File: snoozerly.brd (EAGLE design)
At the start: 70.9 x 44 mm, 51 parts, among them Q2 MOSFET-NCHANNELFDD8780, Q3 MOSFET-NCHANNELBSS123LT1G, Q4 MOSFET-NCHANNELBSS123LT1G, U1 ATMEGA328P, Y1 32KHz, Y2 8MHz

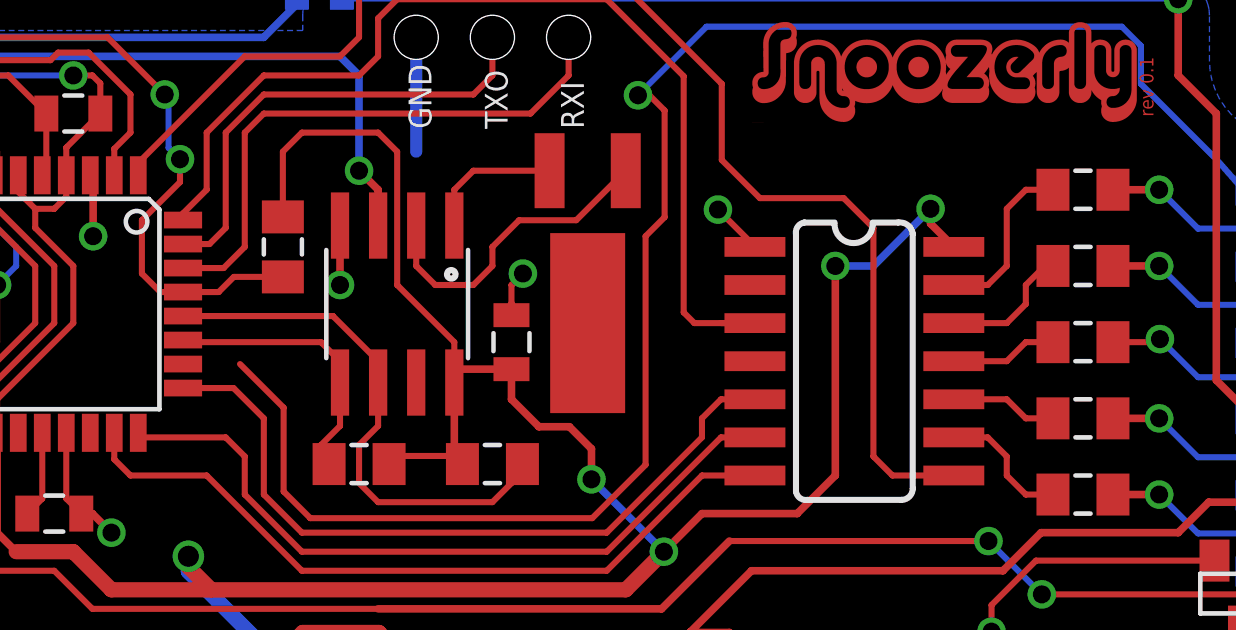
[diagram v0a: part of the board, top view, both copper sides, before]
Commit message: renamed board and schematic files
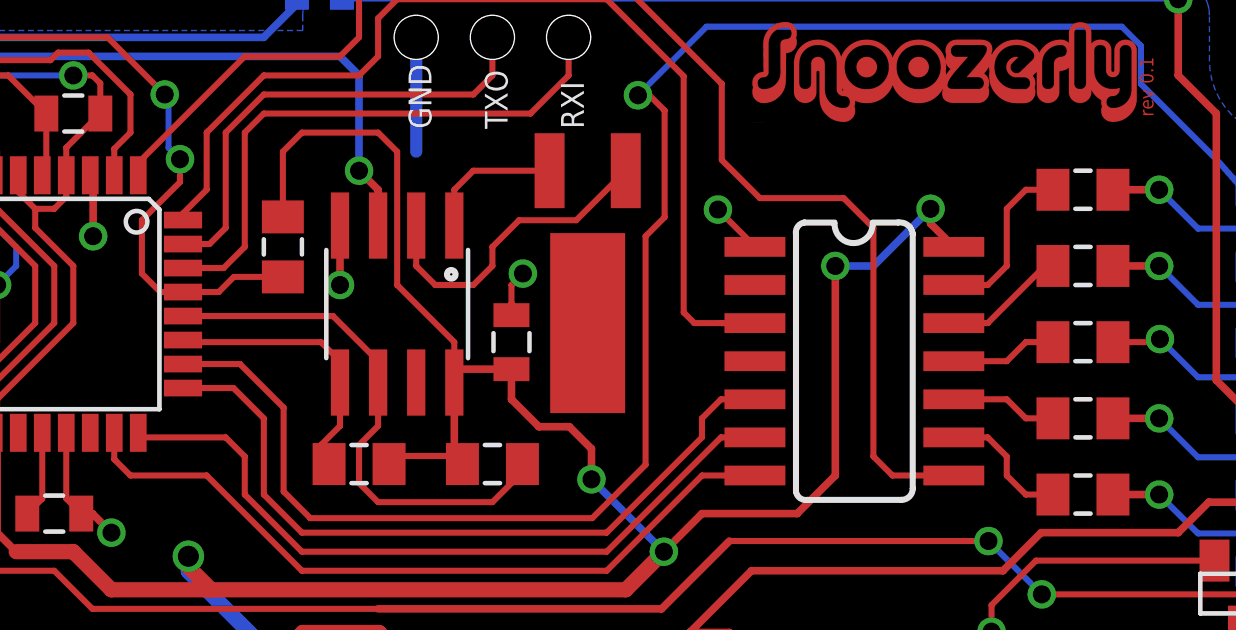
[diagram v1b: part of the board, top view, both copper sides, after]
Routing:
- net STATUS: track 56.9 -> 58.8 mm
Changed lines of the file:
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@@
 <contactref element="AT42QT1070" pad="12"/>
 <contactref element="U$8" pad="1"/>
-<wire x1="54.7243" y1="30.1244" x2="56.4896" y2="30.1244" width="0.2032" layer="1"/>
-<wire x1="56.4896" y1="30.1244" x2="57.1246" y2="30.7594" width="0.2032" layer="1"/>
-<wire x1="57.1246" y1="30.7594" x2="57.1246" y2="31.3944" width="0.2032" layer="1"/>
-<wire x1="57.1246" y1="31.3944" x2="57.7596" y2="32.0294" width="0.2032" layer="1"/>
-<wire x1="57.7596" y1="32.0294" x2="58.0296" y2="32.0294" width="0.2032" layer="1"/>
+<wire x1="58.0296" y1="32.0294" x2="57.7596" y2="32.0294" width="0.2032" layer="1"/>
+<wire x1="57.7596" y1="32.0294" x2="55.8546" y2="30.1244" width="0.2032" layer="1"/>
+<wire x1="55.8546" y1="30.1244" x2="54.7243" y2="30.1244" width="0.2032" layer="1"/>
 </signal>
 <signal name="KEY0">
@@
 <wire x1="63.5" y1="35.56" x2="64.77" y2="34.116" width="0.2032" layer="16"/>
 <wire x1="64.77" y1="34.116" x2="65.612" y2="34.544" width="0.2032" layer="16"/>
-<wire x1="30.9306" y1="28.7594" x2="29.0322" y2="28.7594" width="0" layer="19" extent="1-1"/>
+<wire x1="30.9306" y1="28.7594" x2="29.0322" y2="28.7594" width="0.2032" layer="1"/>
 </signal>
 </signals>

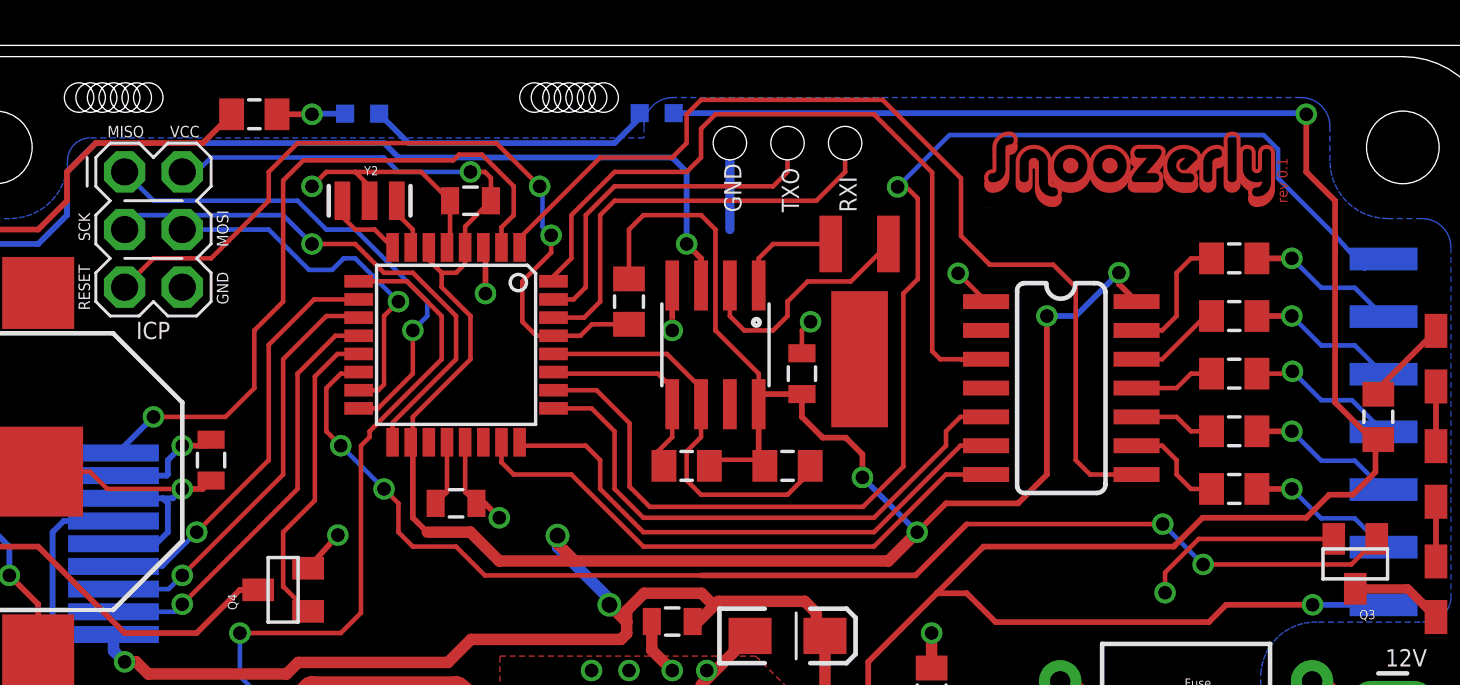
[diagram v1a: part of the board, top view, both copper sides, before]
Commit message: added output 0603 pullup resistors to touch sensor.
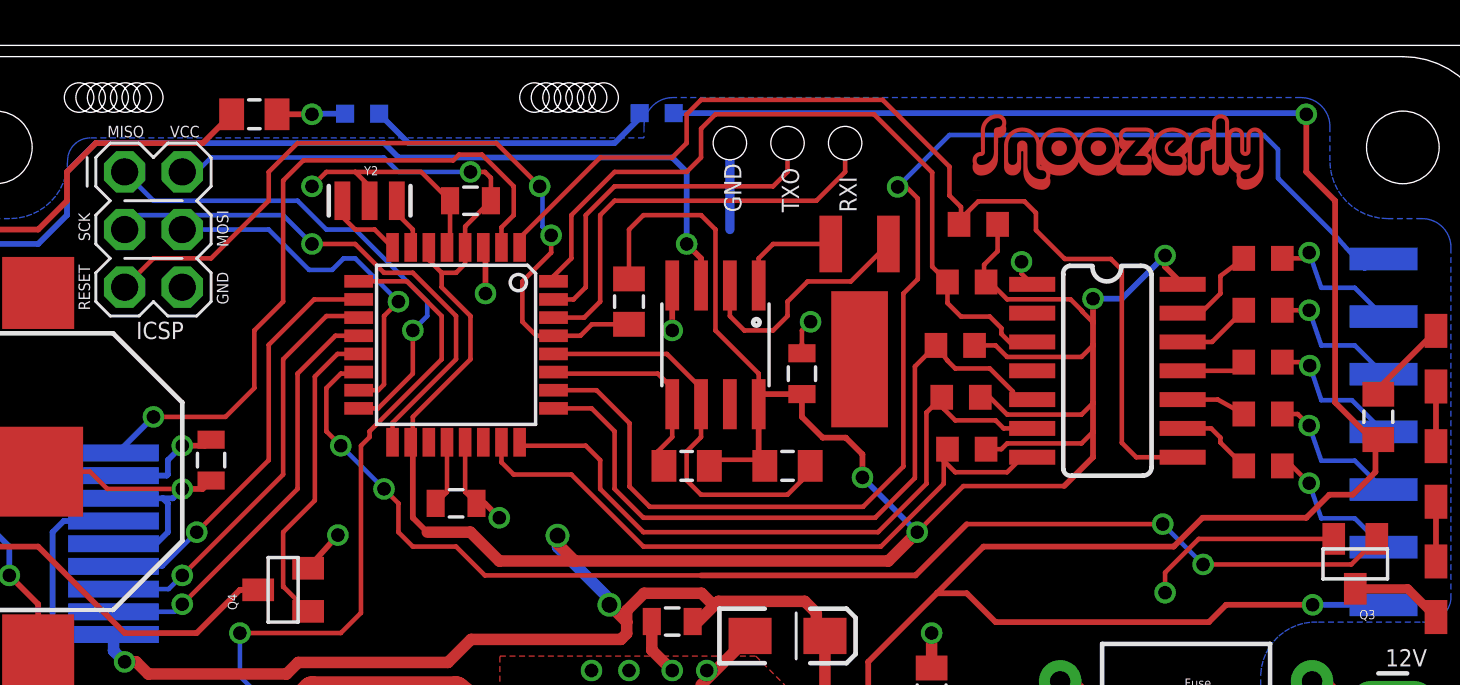
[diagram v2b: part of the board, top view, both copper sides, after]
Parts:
- added U$19: (no value), jt_parts:SNOOZERLY_TOP
- added U$21, U$22, U$23, U$24: 10k, adafruit:R0603
- U$10, U$11, U$7, U$8, U$9: device jt_parts:RESISTOR-0805 -> adafruit:R0603
- U$16: value 103 -> 100
- U$17, U$18: value 330 -> 1.3k
- U$6: value (none) -> 10k; device jt_parts:SNOOZERLY_TOP -> adafruit:R0603
- moved U$6 3.39 mm to (47.2, 33.5), turned to 180 degrees
- moved AT42QT1070 2.17 mm to (53.4, 30.3)
- moved U$11 1.63 mm to (60.3, 25.4)
- moved U$10 1.48 mm to (60.3, 27.7)
- moved U$9 1.37 mm to (60.3, 30.0)
- moved U$8 1.30 mm to (60.3, 32.3)
- moved U$7 1.27 mm to (60.3, 34.6)
- renumbered ICP to ICSP
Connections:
- net 5V: now also U$21.1, U$22.1, U$23.2, U$24.1, U$6.1
- net OUT0: now also U$6.2
- net OUT1: now also U$23.1
- net OUT2: now also U$22.2
- net OUT3: now also U$21.2
- net OUT4: now also U$24.2
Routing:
- net 5V: track 164.4 -> 191.3 mm
- net OUT4: track 24.8 -> 31.9 mm
- net OUT3: track 24.5 -> 30.1 mm
- net OUT2: track 25.1 -> 29.0 mm
- net OUT1: track 43.7 -> 46.6 mm
- net KEY0: track 6.01 -> 4.08 mm
- net KEY4: track 4.74 -> 3.50 mm
- net KEY1: track 4.09 -> 3.27 mm
- net KEY3: track 3.57 -> 2.86 mm
- net OUT0: track 34.3 -> 35.0 mm
- net KEY2: track 3.93 -> 3.36 mm
- net GND: track 115.6 -> 115.1 mm
- net N$30: track 6.65 -> 6.09 mm
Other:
- board text removed: "rev 0.1"

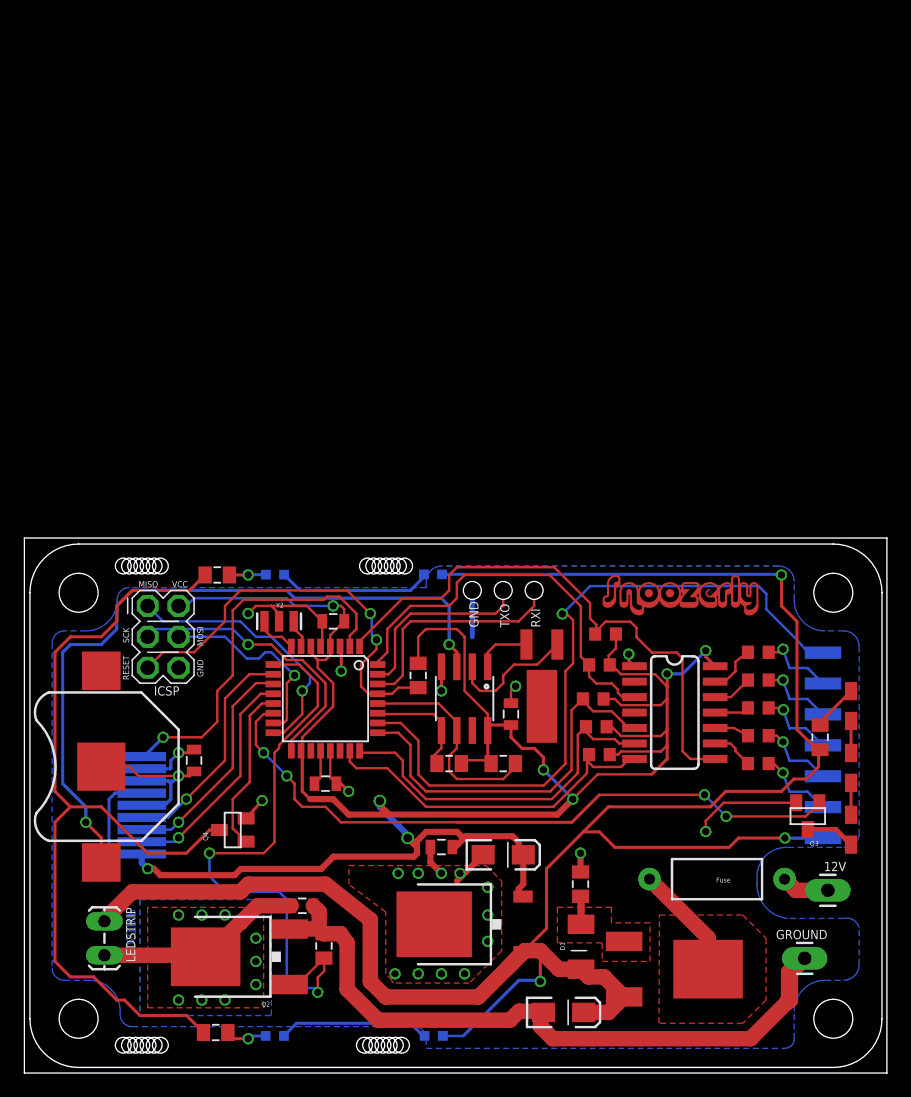
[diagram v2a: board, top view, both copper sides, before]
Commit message: Added electrolytics and snubber jumper.
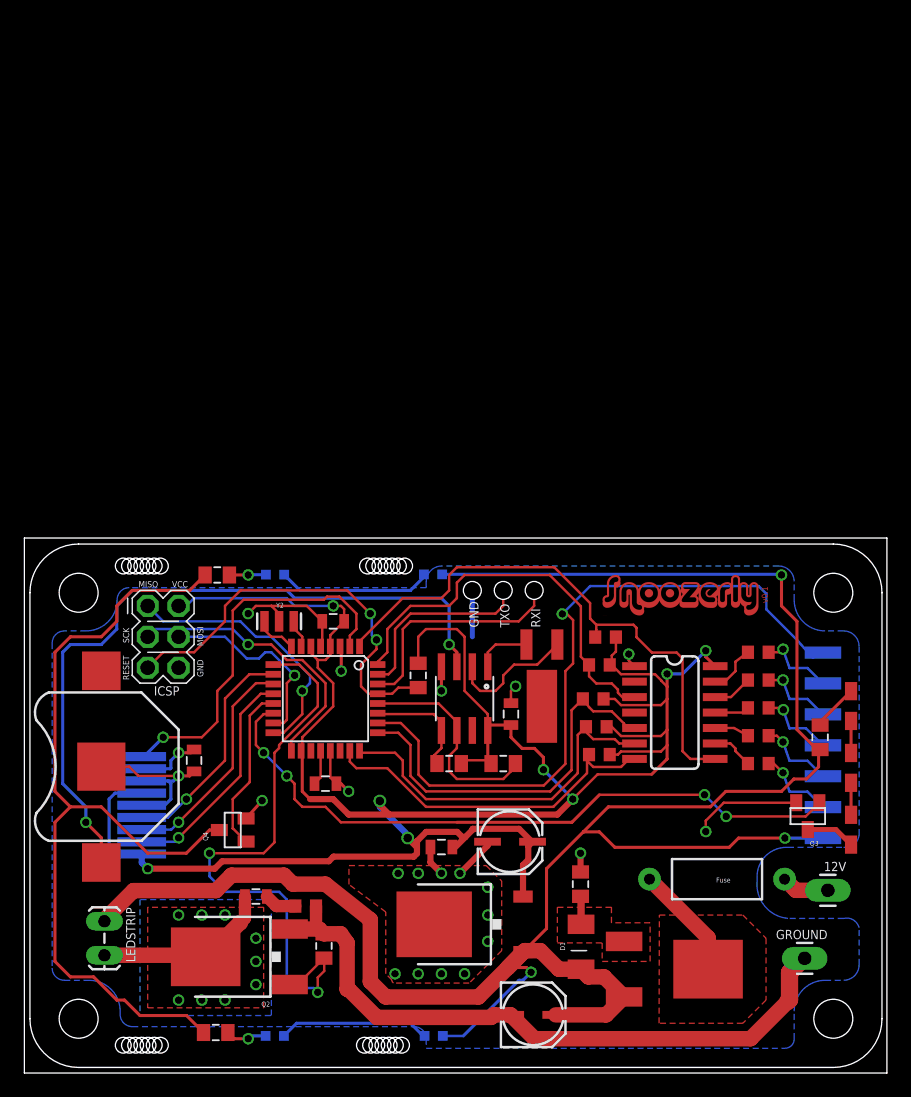
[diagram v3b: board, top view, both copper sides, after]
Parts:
- added U$25: zero, adafruit:R0603
- C5, C7: device SparkFun-Capacitors:EIA3216-KIT -> SparkFun-Capacitors:PANASONIC_C
- moved C4 3.89 mm to (19.0, 14.5)
- moved C5 2.54 mm to (41.8, 4.98)
- moved C7 1.37 mm to (39.9, 19.2)
- moved U$23 0.25 mm to (47.8, 35.8), turned to 180 degrees
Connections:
- new net N$18: C4.1, U$25.2
- net 12V: now also C5.+; no longer C5.A
- net 5V: now also C7.+, U$23.1; no longer C7.A, U$23.2
- net GND: now also C5.-, C7.-, U$25.1; no longer C4.1, C5.C, C7.C
- net OUT1: now also U$23.2; no longer U$23.1
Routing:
- net N$18: track 0.00 -> 2.67 mm
- net N$14: track 19.1 -> 16.6 mm
- net 12V: track 173.1 -> 175.0 mm
- net GND: track 115.1 -> 113.9 mm
- net 5V: track 191.3 -> 192.1 mm
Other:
- board text added: "v0.1"

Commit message: added top control board.
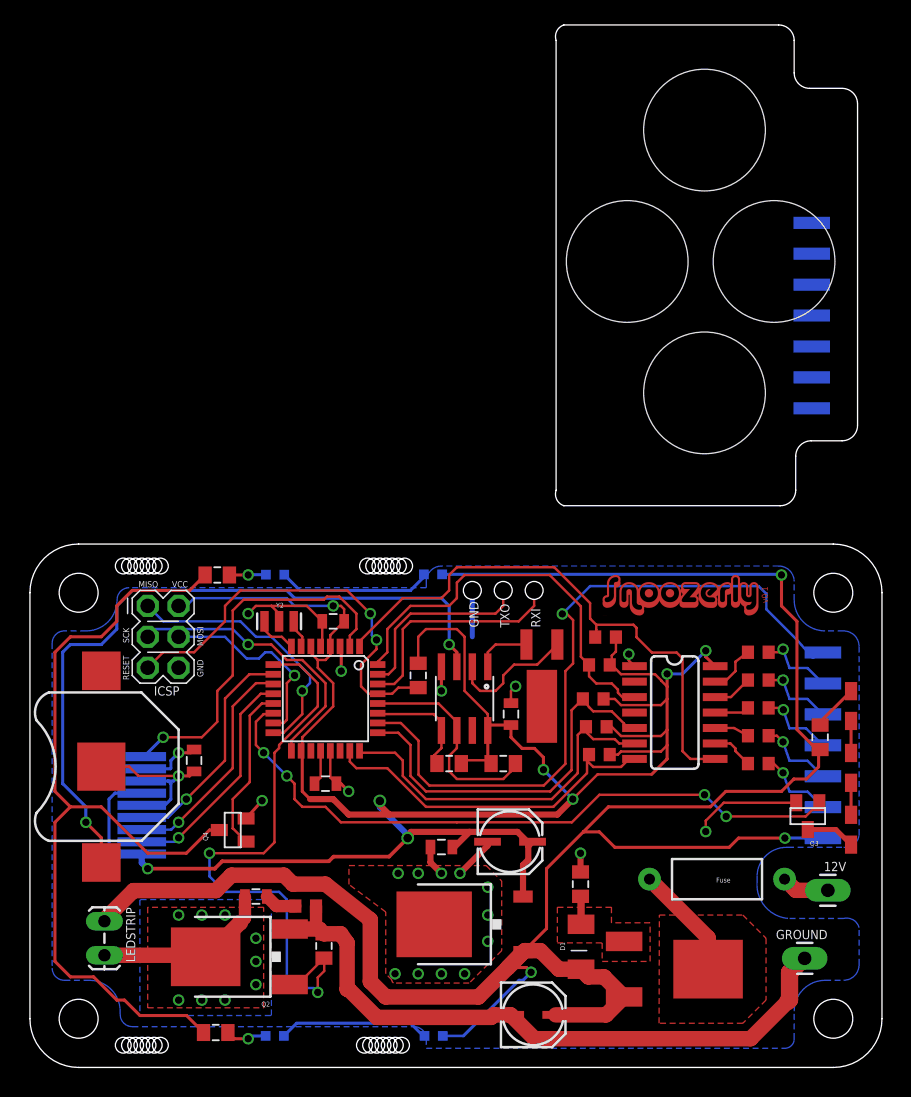
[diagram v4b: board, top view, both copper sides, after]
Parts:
- added U$26: M07, jt_parts:M07-SMD
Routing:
- net 5V: track 192.1 -> 190.5 mm
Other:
- board size 70.9 x 44 mm -> 70 x 43 mm

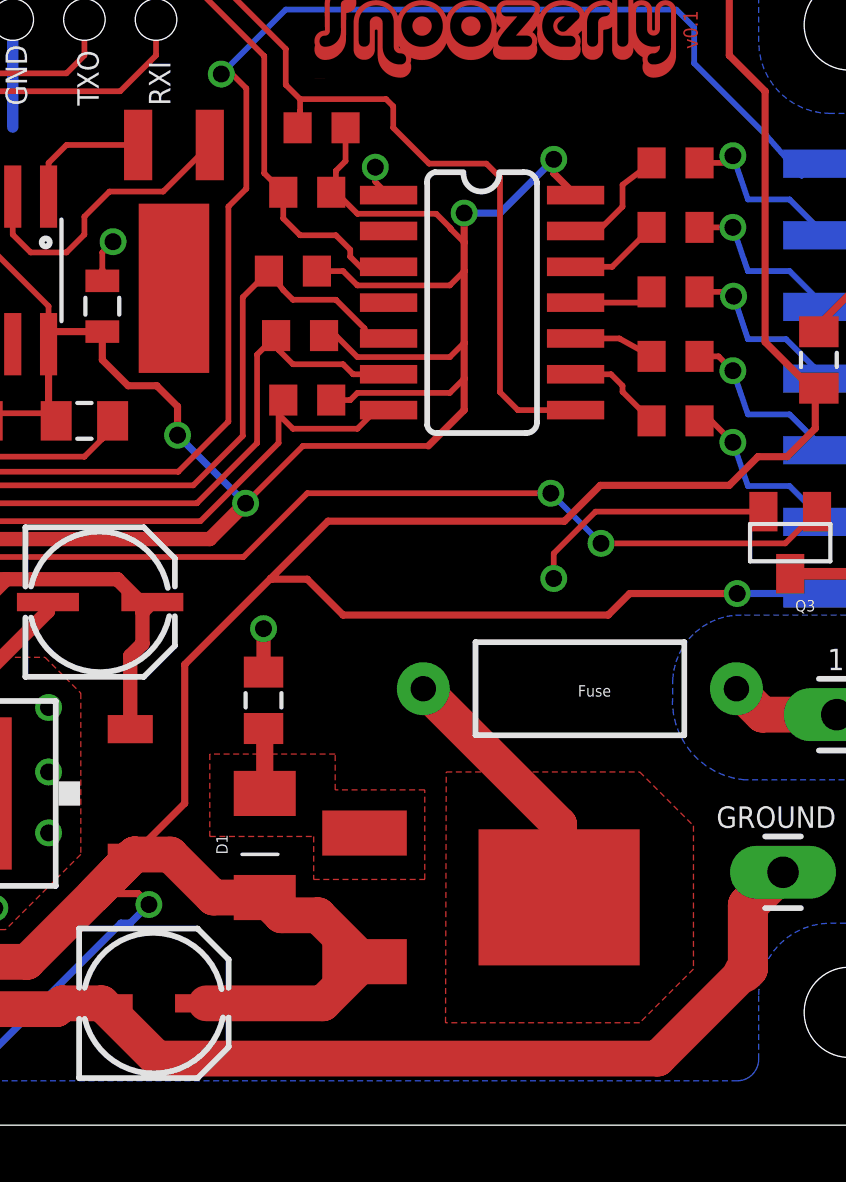
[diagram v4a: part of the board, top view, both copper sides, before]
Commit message: updated diode and SO-14 footprint
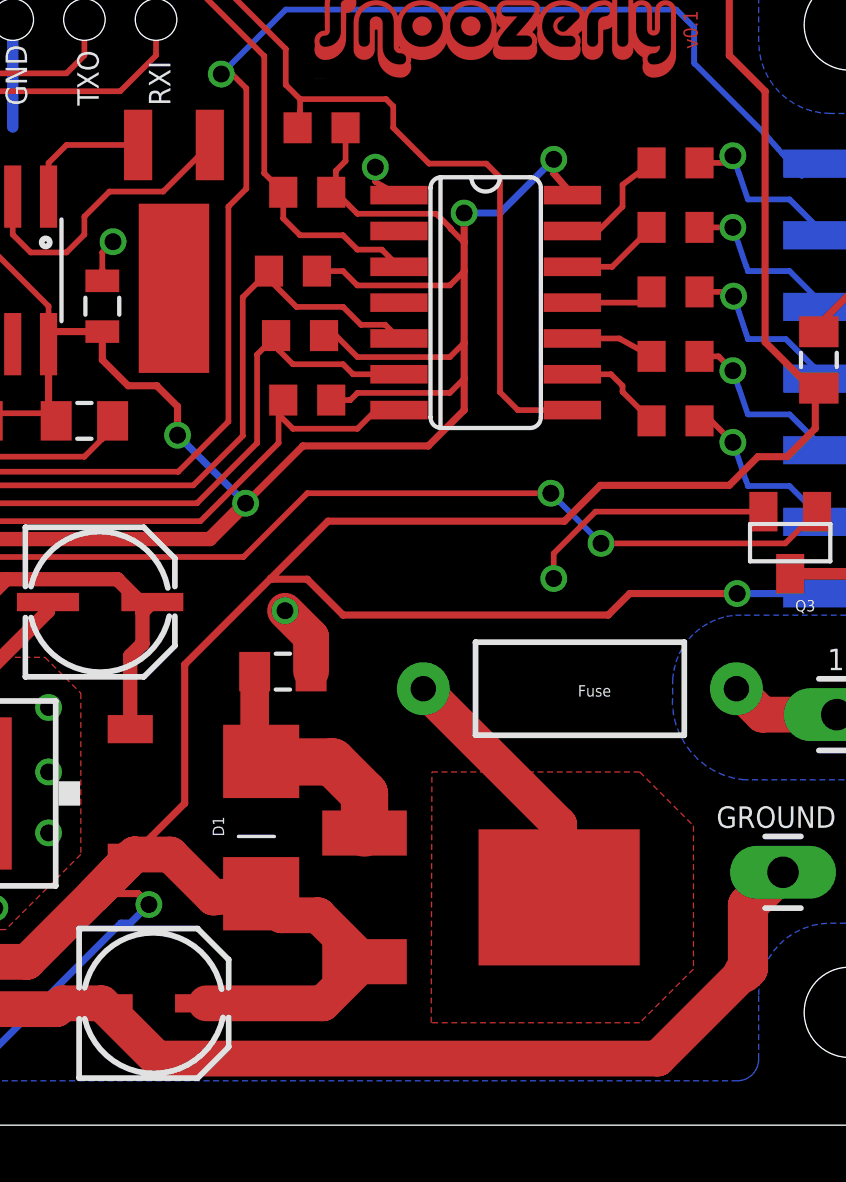
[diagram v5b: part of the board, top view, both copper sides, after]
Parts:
- AT42QT1070: value AT42QT1070 -> AT42QT1070SO-14; device jt_parts:SOIC-14 -> jt_parts:SO-14
- moved U$14 1.23 mm to (46.4, 16.5), turned to 180 degrees
- moved AT42QT1070 0.65 mm to (53.6, 29.6)
- moved D1 0.65 mm to (45.4, 10.7)
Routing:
- net N$16: track 2.32 -> 8.80 mm
- net GND: track 113.9 -> 115.2 mm
- removed copper zone on layer 1, net N$16

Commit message: before remove daughter board
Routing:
- net 5V: track 190.4 -> 191.2 mm

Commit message: before modifying vreg footprint
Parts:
- removed U$26: M07, jt_parts:M07-SMD
- SERIAL: device SparkFun-Connectors:1X03_PP_HOLES_ONLY -> SparkFun-Connectors:1X03_NO_SILK
- moved SERIAL 0.72 mm to (37.3, 39.1)
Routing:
- net GND: track 115.1 -> 111.3 mm
- net OUT0: track 34.8 -> 33.6 mm
- net N$19: track 6.35 -> 5.74 mm
